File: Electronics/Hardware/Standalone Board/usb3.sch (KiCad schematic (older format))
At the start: 0 parts

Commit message: Add rtc, pcie + mipi dsi high level connection, usb 2.0, usb 3.0 and remove audio section
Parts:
- added C? (x22): 0.1uF, symbol Device:C
- added C? (x2): 1uF, symbol Device:C
- added C? (x2): C, symbol Device:C
- added C?: 10uF, symbol Device:C
- added FB? (x2): 220 @ 100mhz, symbol Device:Ferrite_Bead
- added J? (x2): USB3_A, symbol Connector:USB3_A
- added R? (x3): 1M, symbol Device:R
- added R? (x3): 4.7K, symbol Device:R
- added R?: 90.9K 1%, symbol Device:R
- added R?: 10K 1%, symbol Device:R
- added R?: 1K, symbol Device:R
- added R?: 9.53K 1%, symbol Device:R
- added U?: TUSB8020BIPHP, QFP50P900X900X120-49N, symbol TUSB8020BIPHP:TUSB8020BIPHP
- added Y?: 24mhz, symbol Device:Crystal
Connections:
- new net: J?.10 (SHIELD), J?.7 (DRAIN), R?.1 (x2)
- new net: C?.2, FB?.2, J?.1 (VBUS) (x2)
- new net: C?.1, J?.8 (SSTX-) (x2)
- new net: C?.1, J?.9 (SSTX+) (x2)
- new net: R?.1, U?.10 (TEST)
- new net: C?.1, U?.11 (GRSTZ)
- new net: R?.1, U?.21 (PWRCRL_POL/SS_DN1)
- new net: R?.1, U?.24 (USB_R1)
- new net: C?.1, U?.28 (USB_SSTXM_UP)
- new net: C?.1, U?.29 (USB_SSTXP_UP)
- new net: R?.1, U?.35 (GANGED/SMBA2/HS_UP)
- new net: R?.1, U?.36 (FULLPWRMGMTZ/SMBA1/SS_UP)
- new net: C?.2, R?.1, U?.38 (XI), Y?.1
- new net: C?.2, R?.2, U?.39 (XO), Y?.2
- new net: R?.1, R?.1, U?.9 (USB_VBUS)
- new net +3V3: C?.1, C?.1, C?.1, C?.1, C?.1, C?.1, C?.1, C?.1, C?.1, U?.13 (VDD33), U?.23 (VDD33), U?.25 (VDD33), U?.33 (VDD33), U?.37 (VDD33), U?.40 (VDD33), U?.48 (VDD33), U?.5 (OVERCUR1Z), U?.7 (VDD33), U?.8 (OVERCUR2Z)
- new net +5V: FB?.1, FB?.1, R?.2
- new net 1V1: C?.1, C?.1, C?.1, C?.1, C?.1, C?.1, C?.1, U?.1 (VDD), U?.12 (VDD), U?.18 (VDD), U?.30 (VDD), U?.34 (VDD), U?.45 (VDD)
- new net GND: C?.1, C?.1, C?.1, C?.1, C?.2, C?.2, C?.2, C?.2, C?.2, C?.2, C?.2, C?.2, C?.2, C?.2, C?.2, C?.2, C?.2, C?.2, C?.2, C?.2, C?.2, J?.4 (GND), J?.4 (GND), R?.2, R?.2, R?.2, R?.2, R?.2, R?.2, R?.2, R?.2, U?.49 (GND)
- new net USB0_D_N: J?.2 (D-), U?.41 (USB_DP_DN1)
- new net USB0_D_P: J?.3 (D+), U?.42 (USB_DM_DN1)
- new net USB0_SSRX_N: J?.5 (SSRX-), U?.47 (USB_SSRXM_DN1)
- new net USB0_SSRX_P: J?.6 (SSRX+), U?.46 (USB_SSRXP_DN1)
- new net USB0_SSTX_N: C?.2, U?.43 (USB_SSTXP_DN1)
- new net USB0_SSTX_P: C?.2, U?.44 (USB_SSTXM_DN1)
- new net USB1_D_N: J?.2 (D-), U?.15 (USB_DM_DN2)
- new net USB1_D_P: J?.3 (D+), U?.14 (USB_DP_DN2)
- new net USB1_SSRX_N: J?.5 (SSRX-), U?.20 (USB_SSRXM_DN2)
- new net USB1_SSRX_P: J?.6 (SSRX+), U?.19 (USB_SSRXP_DN2)
- new net USB1_SSTX_N: C?.2, U?.17 (USB_SSTXM_DN2)
- new net USB1_SSTX_P: C?.2, U?.16 (USB_SSTXP_DN2)
- new net USB_D_N: U?.27 (USB_DM_UP)
- new net USB_D_P: U?.26 (USB_DP_UP)
- new net USB_SSRX_N: U?.31 (USB_SSRXM_UP)
- new net USB_SSRX_P: U?.32 (USB_SSRXP_UP)
- new net USB_SSTX_N: C?.2
- new net USB_SSTX_P: C?.2
- no-connect marks 0 -> 5
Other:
- note added: "TODO : current limiter"

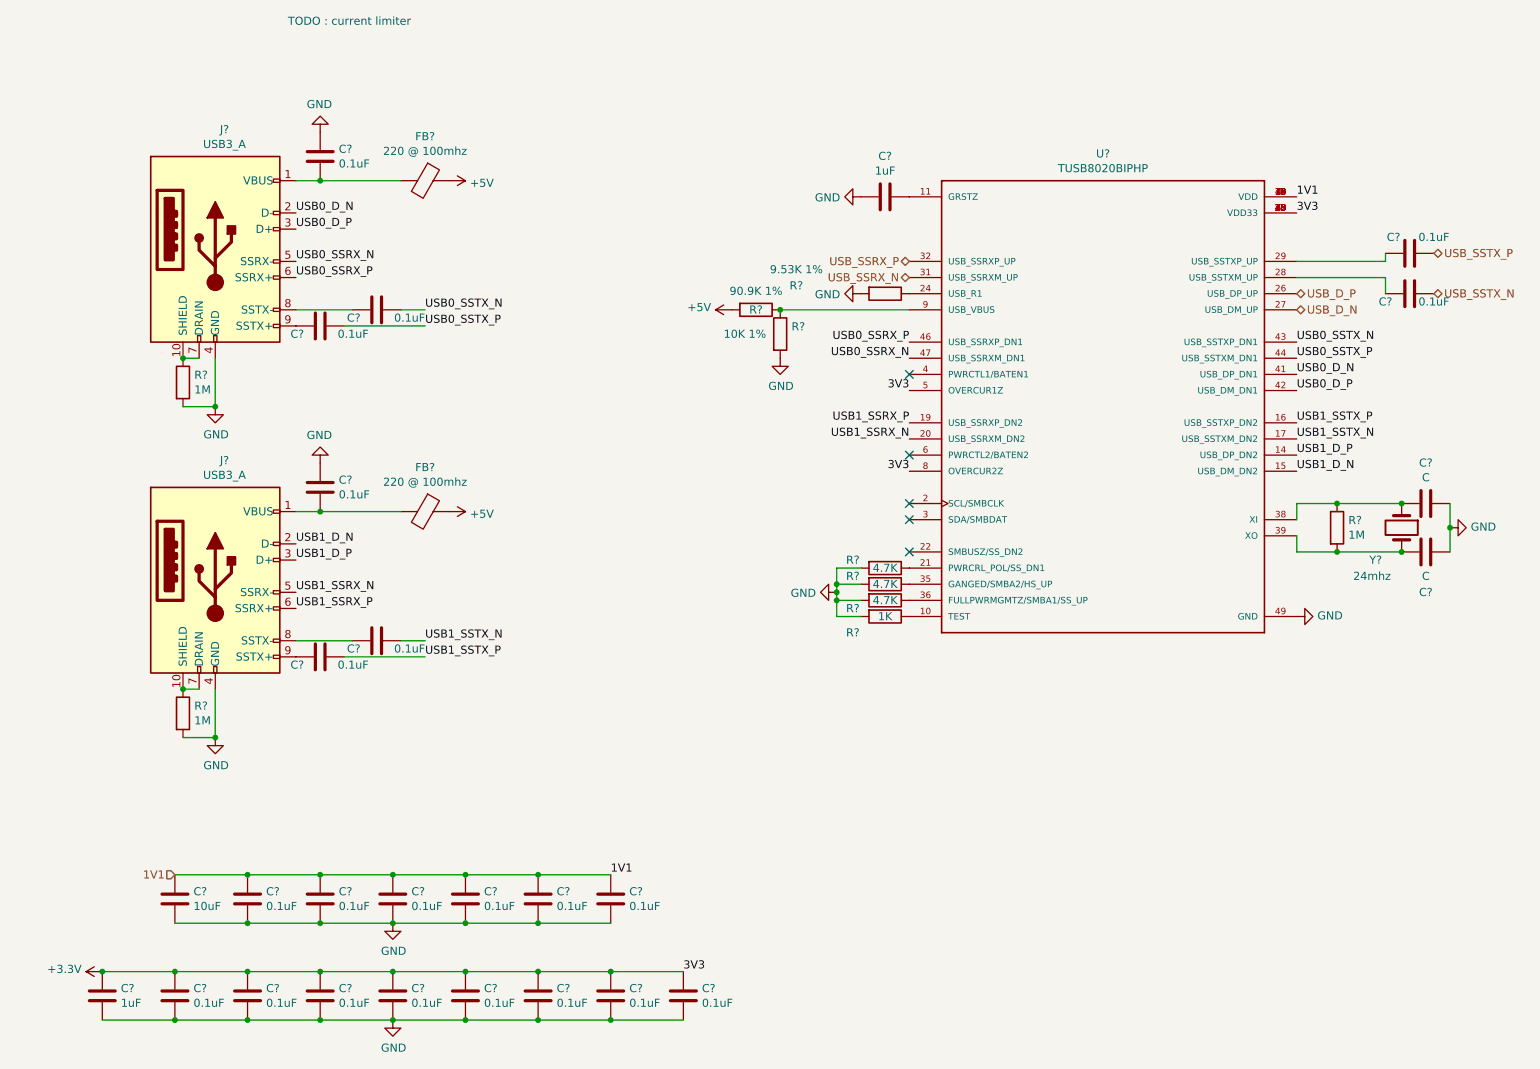
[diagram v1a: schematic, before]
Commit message: Everything is routed, TODO : lenghtmatching + impedance matching + cleaning
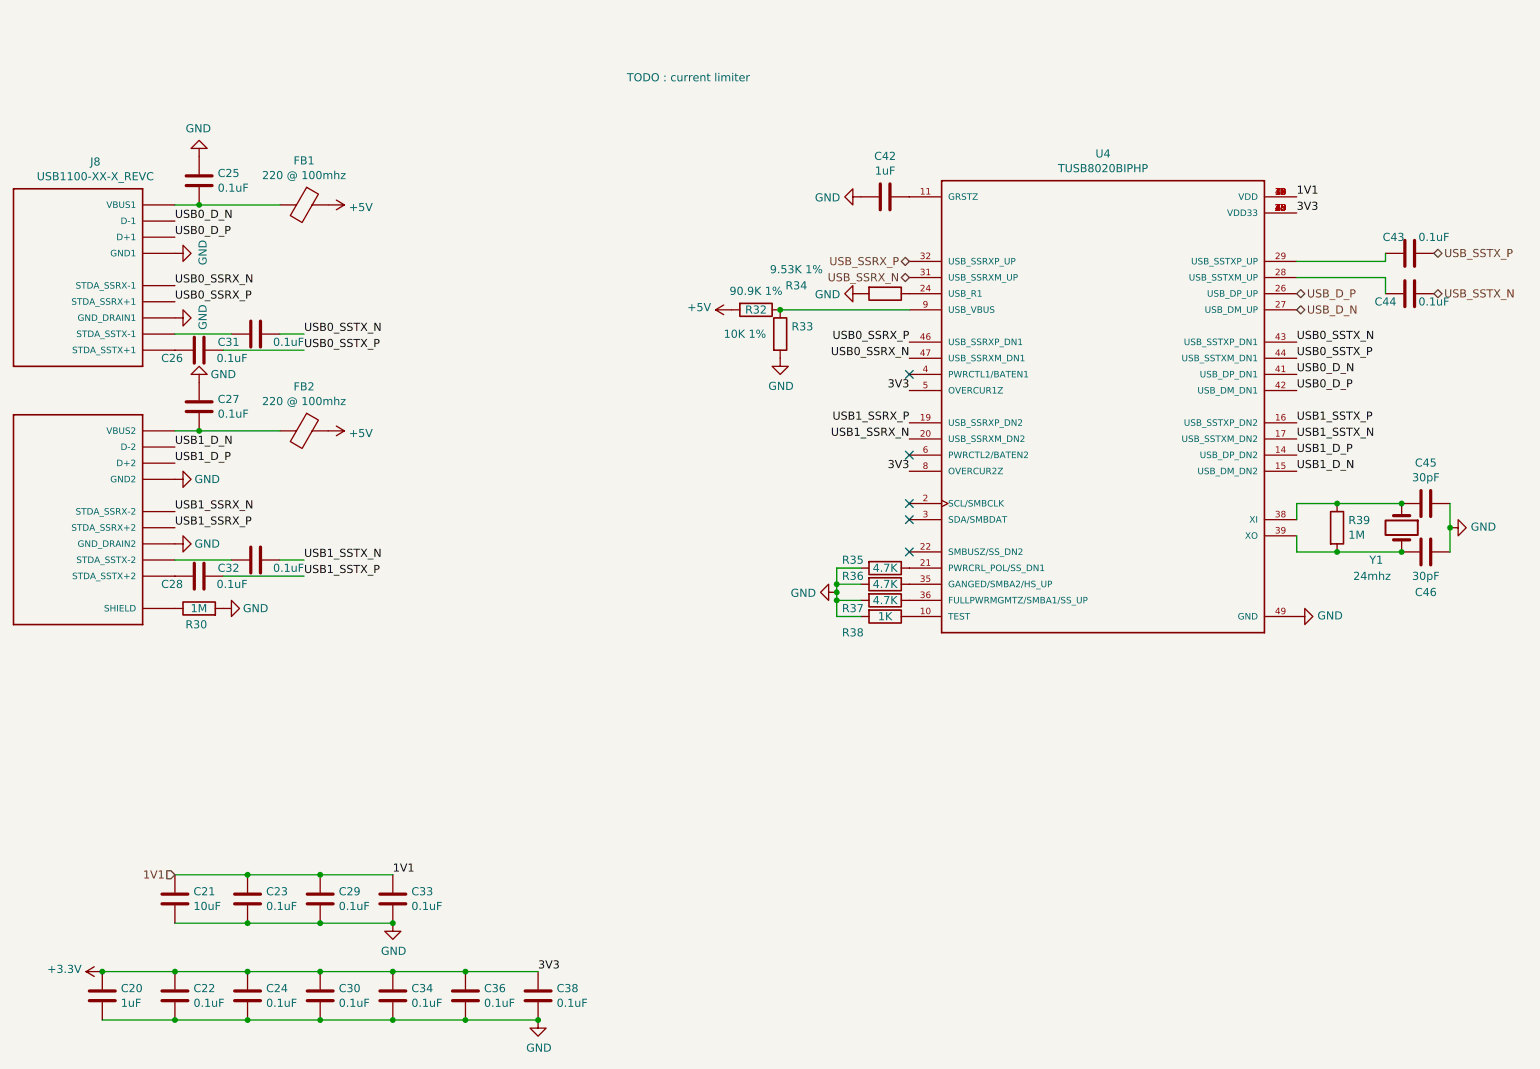
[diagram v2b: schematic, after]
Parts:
- removed C? (x5): 0.1uF, symbol Device:C
- removed J? (x2): USB3_A, symbol Connector:USB3_A
- removed R?: 1M, symbol Device:R
- added J8: USB1100-XX-X_REVC, sb:GCT_USB1100-XX-X_REVC, symbol USB1100-XX-X_REVC:USB1100-XX-X_REVC
- C20, C21, C22, C23, C24, C25, C26, C27, C28, C29, C30, C31, C32, C33, C34, C36, C38, C42, C43, C44: renamed from C?; footprint (none) -> Capacitor_SMD:C_0402_1005Metric
- C45, C46: renamed from C?; value C -> 30pF; footprint (none) -> Capacitor_SMD:C_0402_1005Metric
- FB1, FB2: renamed from FB?; footprint (none) -> Inductor_SMD:L_0402_1005Metric
- R30, R32, R33, R34, R35, R36, R37, R38, R39: renamed from R?; footprint (none) -> Resistor_SMD:R_0201_0603Metric
- U4: renamed from U?; footprint QFP50P900X900X120-49N -> TUSB8020BIPHP:QFP50P900X900X120-49N
- Y1: renamed from Y?; footprint (none) -> Crystal:Crystal_SMD_HC49-SD
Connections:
- net GND: now also J8.13 (GND2), J8.16 (GND_DRAIN2), J8.4 (GND1), J8.7 (GND_DRAIN1)
- net USB0_D_N: now also J8.2 (D-1)
- net USB0_D_P: now also J8.3 (D+1)
- net USB0_SSRX_N: now also J8.5 (STDA_SSRX-1)
- net USB0_SSRX_P: now also J8.6 (STDA_SSRX+1)
- net USB1_D_N: now also J8.11 (D-2)
- net USB1_D_P: now also J8.12 (D+2)
- net USB1_SSRX_N: now also J8.14 (STDA_SSRX-2)
- net USB1_SSRX_P: now also J8.15 (STDA_SSRX+2)
- net at R30.1: now also J8.19 (SHIELD), J8.20 (SHIELD), J8.21 (SHIELD), J8.22 (SHIELD)
- net at C25.2, FB1.2: now also J8.1 (VBUS1)
- net at C27.2, FB2.2: now also J8.10 (VBUS2)
- net at C31.1: now also J8.8 (STDA_SSTX-1)
- net at C26.1: now also J8.9 (STDA_SSTX+1)
- net at C32.1: now also J8.17 (STDA_SSTX-2)
- net at C28.1: now also J8.18 (STDA_SSTX+2)
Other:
- moved on the sheet: C25, C26, C27, C28, C31, C32, FB1, FB2, R30
